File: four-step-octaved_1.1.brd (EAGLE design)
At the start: 95.2 x 42.2 mm, 39 parts, among them IC1 556, IC2 4017N, IC3 4040N, J1 -BATTERY+, J2 SPEAKER, U1 LM386N

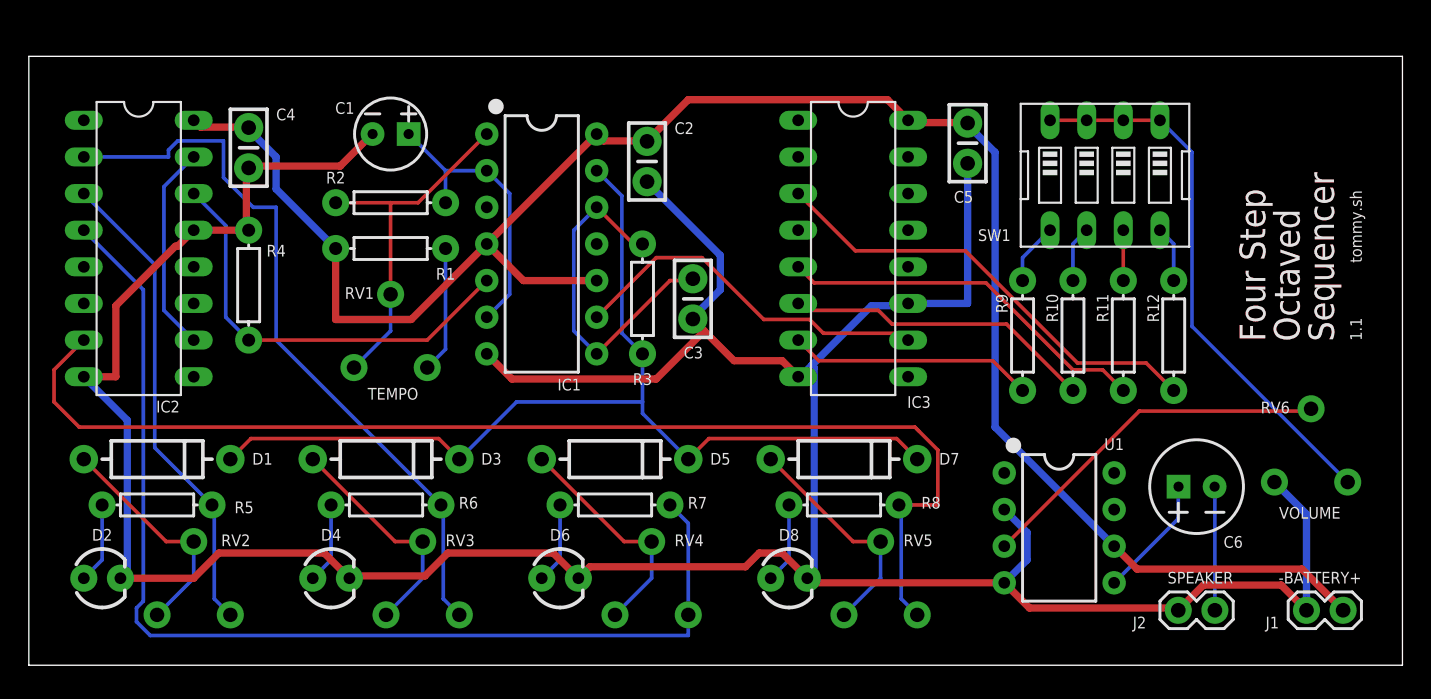
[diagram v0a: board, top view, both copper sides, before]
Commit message: Add mounting holes, increment version to 1.1.1
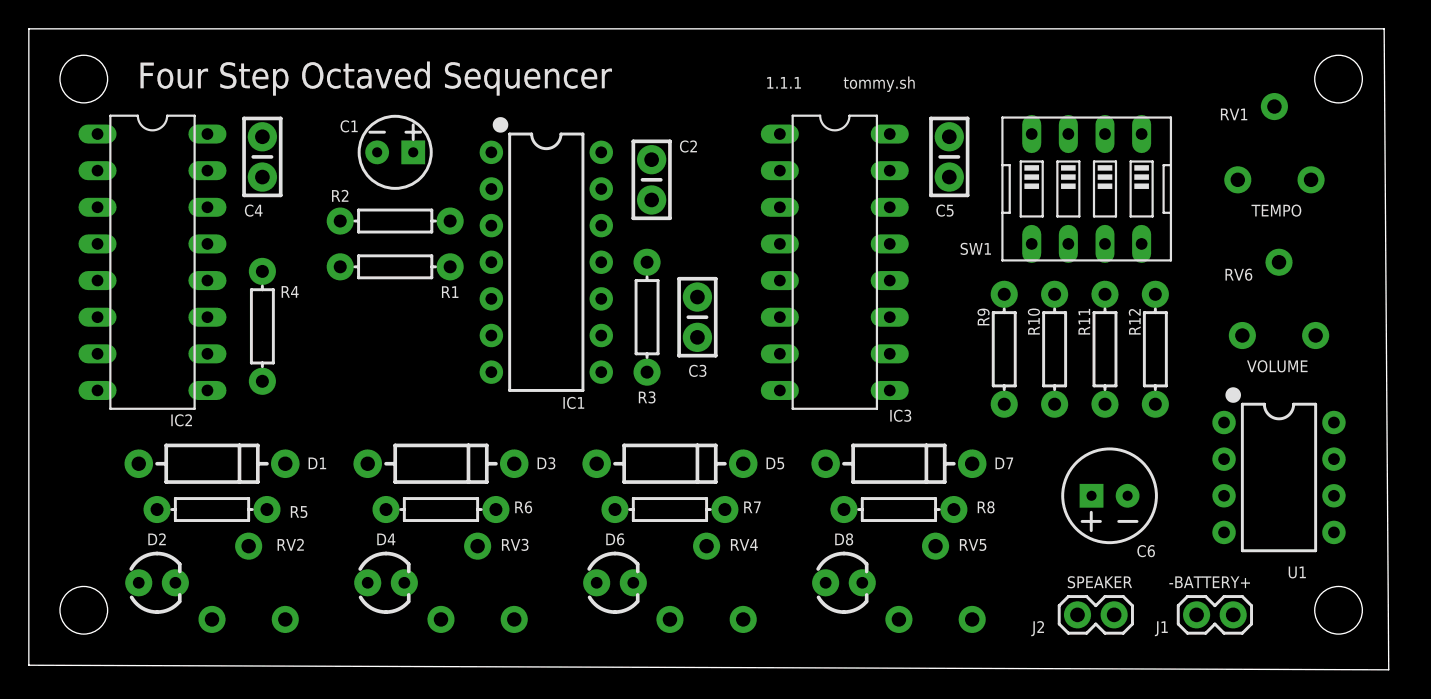
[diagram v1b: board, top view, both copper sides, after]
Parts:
- moved RV1 62.6 mm to (86.4, 33.7)
- moved U1 15.6 mm to (86.7, 13.0)
- moved RV6 10.4 mm to (86.7, 22.9)
- moved J1 7.63 mm to (83.5, 3.49)
- moved J2 6.99 mm to (75.2, 3.49)
- moved C6 6.07 mm to (74.9, 11.7)
- moved D4 3.82 mm to (24.8, 5.71)
- moved D5 3.82 mm to (44.5, 14.0)
- moved D6 3.82 mm to (40.6, 5.71)
- moved D7 3.82 mm to (60.3, 14.0)
- moved D8 3.82 mm to (56.5, 5.71)
- moved R7 3.82 mm to (44.5, 10.8)
- moved R8 3.82 mm to (60.3, 10.8)
- moved RV4 3.82 mm to (47.0, 3.17)
- moved RV5 3.82 mm to (62.9, 3.17)
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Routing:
- net GND: track 230.3 -> 0.00 mm
- net +9V: track 131.0 -> 0.00 mm
- net N$10: track 82.5 -> 0.00 mm
- net N$9: track 77.3 -> 0.00 mm
- net N$19: track 71.1 -> 0.00 mm
- net N$8: track 51.0 -> 0.00 mm
- net N$31: track 38.1 -> 0.00 mm
- net N$7: track 33.4 -> 0.00 mm
- net N$25: track 31.7 -> 0.00 mm
- net N$5: track 30.0 -> 0.00 mm
- net N$21: track 26.1 -> 0.00 mm
- net N$43: track 25.7 -> 0.00 mm
- net N$24: track 25.2 -> 0.00 mm
- net N$2: track 24.9 -> 0.00 mm
- net N$6: track 24.6 -> 0.00 mm
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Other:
- board size 95.2 x 42.2 mm -> 94.3 x 44.4 mm
- board text added: "1.1.1"
- board text removed: "1.1"
